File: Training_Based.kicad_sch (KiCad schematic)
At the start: 6 parts

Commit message: update
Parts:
- added K (x2): FINDER-36.11, Relay_THT:Relay_SPDT_Finder_36.11, symbol Relay:FINDER-36.11
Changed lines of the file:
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@@
     (pin "1")
+  )
+  (symbol (lib_id "Relay:FINDER-36.11") (at 52.705 45.085 0) (unit 1)
+    (in_bom yes) (on_board yes) (fields_autoplaced)
+    (default_instance (reference "K") (unit 1) (value "FINDER-36.11") (footprint "Relay_THT:Relay_SPDT_Finder_36.11"))
+    (property "Reference" "K" (id 0) (at 64.77 44.45 0)
+      (effects (font (size 1.27 1.27)) (justify left))
+    )
+    (property "Value" "FINDER-36.11" (id 1) (at 64.77 46.99 0)
+      (effects (font (size 1.27 1.27)) (justify left))
+    )
+    (property "Footprint" "Relay_THT:Relay_SPDT_Finder_36.11" (id 2) (at 84.963 45.847 0)
+      (effects (font (size 1.27 1.27)) hide)
+    )
+    (property "Datasheet" "https://gfinder.findernet.com/public/attachments/36/EN/S36EN.pdf" (id 3) (at 52.705 45.085 0)
+      (effects (font (size 1.27 1.27)) hide)
+    )
+    (pin "11")
+    (pin "12")
+    (pin "14")
+    (pin "A1")
+    (pin "A2")
   )
   (symbol (lib_id "power:GND") (at 255.905 150.495 0) (unit 1)
@@
     (pin "1")
   )
+  (symbol (lib_id "Relay:FINDER-36.11") (at 52.705 64.77 0) (unit 1)
+    (in_bom yes) (on_board yes) (fields_autoplaced)
+    (default_instance (reference "K") (unit 1) (value "FINDER-36.11") (footprint "Relay_THT:Relay_SPDT_Finder_36.11"))
+    (property "Reference" "K" (id 0) (at 64.77 64.135 0)
+      (effects (font (size 1.27 1.27)) (justify left))
+    )
+    (property "Value" "FINDER-36.11" (id 1) (at 64.77 66.675 0)
+      (effects (font (size 1.27 1.27)) (justify left))
+    )
+    (property "Footprint" "Relay_THT:Relay_SPDT_Finder_36.11" (id 2) (at 84.963 65.532 0)
+      (effects (font (size 1.27 1.27)) hide)
+    )
+    (property "Datasheet" "https://gfinder.findernet.com/public/attachments/36/EN/S36EN.pdf" (id 3) (at 52.705 64.77 0)
+      (effects (font (size 1.27 1.27)) hide)
+    )
+    (pin "11")
+    (pin "12")
+    (pin "14")
+    (pin "A1")
+    (pin "A2")
+  )
   (sheet_instances
     (path "/" (page "1"))
@@
       (reference "H6") (unit 1) (value "MountingHole_Pad") (footprint "MountingHole:MountingHole_3.2mm_M3_Pad_Via")
     )
+    (path "/0bf7dc38-c684-4e7e-b8ab-62403329c020"
+      (reference "K1") (unit 1) (value "FINDER-36.11") (footprint "Relay_THT:Relay_SPDT_Finder_36.11")
+    )
+    (path "/f917dee2-fb9b-4968-83ae-cd84153be184"
+      (reference "K2") (unit 1) (value "FINDER-36.11") (footprint "Relay_THT:Relay_SPDT_Finder_36.11")
+    )
   )

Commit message: update
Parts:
- added BZ: Buzzer, symbol Device:Buzzer
- added U: HC-SR04, symbol hc-sr04:HC-SR04
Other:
- moved on the sheet: K
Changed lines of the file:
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@@
     (pin "1")
   )
-  (symbol (lib_id "Relay:FINDER-36.11") (at 52.705 45.085 0) (unit 1)
+  (symbol (lib_id "Relay:FINDER-36.11") (at 52.705 46.99 0) (unit 1)
     (in_bom yes) (on_board yes) (fields_autoplaced)
     (default_instance (reference "K") (unit 1) (value "FINDER-36.11") (footprint "Relay_THT:Relay_SPDT_Finder_36.11"))
-    (property "Reference" "K" (id 0) (at 64.77 44.45 0)
-      (effects (font (size 1.27 1.27)) (justify left))
-    )
-    (property "Value" "FINDER-36.11" (id 1) (at 64.77 46.99 0)
-      (effects (font (size 1.27 1.27)) (justify left))
-    )
-    (property "Footprint" "Relay_THT:Relay_SPDT_Finder_36.11" (id 2) (at 84.963 45.847 0)
-      (effects (font (size 1.27 1.27)) hide)
-    )
-    (property "Datasheet" "https://gfinder.findernet.com/public/attachments/36/EN/S36EN.pdf" (id 3) (at 52.705 45.085 0)
+    (property "Reference" "K" (id 0) (at 64.77 46.355 0)
+      (effects (font (size 1.27 1.27)) (justify left))
+    )
+    (property "Value" "FINDER-36.11" (id 1) (at 64.77 48.895 0)
+      (effects (font (size 1.27 1.27)) (justify left))
+    )
+    (property "Footprint" "Relay_THT:Relay_SPDT_Finder_36.11" (id 2) (at 84.963 47.752 0)
+      (effects (font (size 1.27 1.27)) hide)
+    )
+    (property "Datasheet" "https://gfinder.findernet.com/public/attachments/36/EN/S36EN.pdf" (id 3) (at 52.705 46.99 0)
       (effects (font (size 1.27 1.27)) hide)
     )
@@
     (pin "1")
   )
+  (symbol (lib_id "Device:Buzzer") (at 146.685 47.625 0) (unit 1)
+    (in_bom yes) (on_board yes) (fields_autoplaced)
+    (default_instance (reference "BZ") (unit 1) (value "Buzzer") (footprint ""))
+    (property "Reference" "BZ" (id 0) (at 151.13 46.99 0)
+      (effects (font (size 1.27 1.27)) (justify left))
+    )
+    (property "Value" "Buzzer" (id 1) (at 151.13 49.53 0)
+      (effects (font (size 1.27 1.27)) (justify left))
+    )
+    (property "Footprint" "" (id 2) (at 146.05 45.085 90)
+      (effects (font (size 1.27 1.27)) hide)
+    )
+    (property "Datasheet" "~" (id 3) (at 146.05 45.085 90)
+      (effects (font (size 1.27 1.27)) hide)
+    )
+    (pin "1")
+    (pin "2")
+  )
   (symbol (lib_id "Mechanical:MountingHole_Pad") (at 261.62 130.81 270) (unit 1)
     (in_bom yes) (on_board yes)
@@
     )
     (pin "1")
+  )
+  (symbol (lib_id "hc-sr04:HC-SR04") (at 114.3 50.165 0) (unit 1)
+    (in_bom yes) (on_board yes)
+    (default_instance (reference "U") (unit 1) (value "HC-SR04") (footprint ""))
+    (property "Reference" "U" (id 0) (at 123.19 48.895 0)
+      (effects (font (size 1.524 1.524)) (justify left))
+    )
+    (property "Value" "HC-SR04" (id 1) (at 123.19 51.435 0)
+      (effects (font (size 1.524 1.524)) (justify left))
+    )
+    (property "Footprint" "" (id 2) (at 114.935 43.815 0)
+      (effects (font (size 1.524 1.524)))
+    )
+    (property "Datasheet" "" (id 3) (at 116.84 48.895 0)
+      (effects (font (size 1.524 1.524)))
+    )
+    (pin "~")
+    (pin "~")
+    (pin "~")
+    (pin "~")
   )
   (symbol (lib_id "Mechanical:MountingHole_Pad") (at 261.62 125.095 270) (unit 1)
@@
       (reference "#PWR01") (unit 1) (value "GND") (footprint "")
     )
+    (path "/4b249d15-dc1f-4ea2-a810-eeeb52784c39"
+      (reference "BZ1") (unit 1) (value "Buzzer") (footprint "Buzzer_Beeper:Buzzer_12x9.5RM7.6")
+    )
     (path "/bec85d69-b4a6-498e-b897-830e44594378"
       (reference "H1") (unit 1) (value "MountingHole_Pad") (footprint "MountingHole:MountingHole_3.2mm_M3_Pad_Via")
@@
       (reference "K2") (unit 1) (value "FINDER-36.11") (footprint "Relay_THT:Relay_SPDT_Finder_36.11")
     )
-  )
+    (path "/66e603fb-b814-425a-a9e3-3759b5b268a1"
+      (reference "U1") (unit 1) (value "HC-SR04") (footprint "Library:HC-SR04")
+    )
+  )

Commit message: add spacerx6
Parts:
- added AFF (x2): LTS-6980HR, Display_7Segment:7SegmentLED_LTS6760_LTS6780, symbol Display_Character:LTS-6980HR
- added U: Protoboard, symbol Training_board:Protoboard
- added U: DHT11, Sensor:Aosong_DHT11_5.5x12.0_P2.54mm, symbol Sensor:DHT11
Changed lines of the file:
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@@
     (pin "A2")
+  )
+  (symbol (lib_id "Training_board:Protoboard") (at 53.975 104.14 0) (unit 1)
+    (in_bom yes) (on_board yes) (fields_autoplaced)
+    (default_instance (reference "U") (unit 1) (value "Protoboard") (footprint ""))
+    (property "Reference" "U" (id 0) (at 60.96 103.505 0)
+      (effects (font (size 1.27 1.27)) (justify left))
+    )
+    (property "Value" "Protoboard" (id 1) (at 60.96 106.045 0)
+      (effects (font (size 1.27 1.27)) (justify left))
+    )
+    (property "Footprint" "" (id 2) (at 53.975 104.14 0)
+      (effects (font (size 1.27 1.27)) hide)
+    )
+    (property "Datasheet" "" (id 3) (at 53.975 104.14 0)
+      (effects (font (size 1.27 1.27)) hide)
+    )
   )
   (symbol (lib_id "power:GND") (at 255.905 150.495 0) (unit 1)
@@
     (pin "~")
   )
+  (symbol (lib_id "Display_Character:LTS-6980HR") (at 127.635 93.345 0) (unit 1)
+    (in_bom yes) (on_board yes) (fields_autoplaced)
+    (default_instance (reference "AFF") (unit 1) (value "LTS-6980HR") (footprint "Display_7Segment:7SegmentLED_LTS6760_LTS6780"))
+    (property "Reference" "AFF" (id 0) (at 127.635 76.835 0)
+      (effects (font (size 1.27 1.27)))
+    )
+    (property "Value" "LTS-6980HR" (id 1) (at 127.635 79.375 0)
+      (effects (font (size 1.27 1.27)))
+    )
+    (property "Footprint" "Display_7Segment:7SegmentLED_LTS6760_LTS6780" (id 2) (at 127.635 108.585 0)
+      (effects (font (size 1.27 1.27)) hide)
+    )
+    (property "Datasheet" "http://datasheet.octopart.com/LTS-6960HR-Lite-On-datasheet-11803242.pdf" (id 3) (at 127.635 93.345 0)
+      (effects (font (size 1.27 1.27)) hide)
+    )
+    (pin "1")
+    (pin "10")
+    (pin "2")
+    (pin "3")
+    (pin "4")
+    (pin "5")
+    (pin "6")
+    (pin "7")
+    (pin "8")
+    (pin "9")
+  )
+  (symbol (lib_id "Sensor:DHT11") (at 142.875 31.75 0) (unit 1)
+    (in_bom yes) (on_board yes) (fields_autoplaced)
+    (default_instance (reference "U") (unit 1) (value "DHT11") (footprint "Sensor:Aosong_DHT11_5.5x12.0_P2.54mm"))
+    (property "Reference" "U" (id 0) (at 135.89 31.115 0)
+      (effects (font (size 1.27 1.27)) (justify right))
+    )
+    (property "Value" "DHT11" (id 1) (at 135.89 33.655 0)
+      (effects (font (size 1.27 1.27)) (justify right))
+    )
+    (property "Footprint" "Sensor:Aosong_DHT11_5.5x12.0_P2.54mm" (id 2) (at 142.875 41.91 0)
+      (effects (font (size 1.27 1.27)) hide)
+    )
+    (property "Datasheet" "http://akizukidenshi.com/download/ds/aosong/DHT11.pdf" (id 3) (at 146.685 25.4 0)
+      (effects (font (size 1.27 1.27)) hide)
+    )
+    (pin "1")
+    (pin "2")
+    (pin "3")
+    (pin "4")
+  )
   (symbol (lib_id "Mechanical:MountingHole_Pad") (at 261.62 125.095 270) (unit 1)
     (in_bom yes) (on_board yes)
@@
     )
     (pin "1")
+  )
+  (symbol (lib_id "Display_Character:LTS-6980HR") (at 95.885 92.71 0) (unit 1)
+    (in_bom yes) (on_board yes) (fields_autoplaced)
+    (default_instance (reference "AFF") (unit 1) (value "LTS-6980HR") (footprint "Display_7Segment:7SegmentLED_LTS6760_LTS6780"))
+    (property "Reference" "AFF" (id 0) (at 95.885 76.2 0)
+      (effects (font (size 1.27 1.27)))
+    )
+    (property "Value" "LTS-6980HR" (id 1) (at 95.885 78.74 0)
+      (effects (font (size 1.27 1.27)))
+    )
+    (property "Footprint" "Display_7Segment:7SegmentLED_LTS6760_LTS6780" (id 2) (at 95.885 107.95 0)
+      (effects (font (size 1.27 1.27)) hide)
+    )
+    (property "Datasheet" "http://datasheet.octopart.com/LTS-6960HR-Lite-On-datasheet-11803242.pdf" (id 3) (at 95.885 92.71 0)
+      (effects (font (size 1.27 1.27)) hide)
+    )
+    (pin "1")
+    (pin "10")
+    (pin "2")
+    (pin "3")
+    (pin "4")
+    (pin "5")
+    (pin "6")
+    (pin "7")
+    (pin "8")
+    (pin "9")
   )
   (symbol (lib_id "Relay:FINDER-36.11") (at 52.705 64.77 0) (unit 1)
@@
       (reference "#PWR01") (unit 1) (value "GND") (footprint "")
     )
+    (path "/d28ba196-9e7b-40b2-b3ef-8cb68851e10f"
+      (reference "AFF1") (unit 1) (value "LTS-6980HR") (footprint "Display_7Segment:7SegmentLED_LTS6760_LTS6780")
+    )
+    (path "/9d925192-1582-48c4-b69c-59437c278f89"
+      (reference "AFF2") (unit 1) (value "LTS-6980HR") (footprint "Display_7Segment:7SegmentLED_LTS6760_LTS6780")
+    )
     (path "/4b249d15-dc1f-4ea2-a810-eeeb52784c39"
       (reference "BZ1") (unit 1) (value "Buzzer") (footprint "Buzzer_Beeper:Buzzer_12x9.5RM7.6")
@@
       (reference "U1") (unit 1) (value "HC-SR04") (footprint "Library:HC-SR04")
     )
-  )
+    (path "/a1b2256e-71d9-455c-a704-d555bf14e270"
+      (reference "U2") (unit 1) (value "DHT11") (footprint "Sensor:Aosong_DHT11_5.5x12.0_P2.54mm")
+    )
+    (path "/17077e5b-82a4-4c35-a7b1-ed0c3a3a0da8"
+      (reference "U3") (unit 1) (value "Protoboard") (footprint "Library:Protoboard")
+    )
+  )

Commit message: ีWork in Progress
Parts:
- removed U (x2): (no value), symbol Mechanical:MountingHole_Pad
- removed U: DHT11, Sensor:Aosong_DHT11_5.5x12.0_P2.54mm, symbol Sensor:DHT11
- added J (x4): Conn_01x19, symbol Connector_Generic:Conn_01x19
- added PIR: PIR_Motion_Sensor, symbol sensors:PIR_Motion_Sensor
- added Q: BC817, Package_TO_SOT_SMD:SOT-23, symbol Transistor_BJT:BC817
- added TH: DHT11_Temperature_Humidity, symbol sensors:DHT11_Temperature_Humidity
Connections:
- net GND: now also Q.2 (E)
- net +5V: now reaches BZ.1 (-)
- net at BZ.2 (+): now also Q.3 (C)
- new net: J.1 (Pin_1), J.1 (Pin_1) (x2)
- new net: J.10 (Pin_10), J.10 (Pin_10) (x2)
- new net: J.11 (Pin_11), J.11 (Pin_11) (x2)
- new net: J.12 (Pin_12), J.12 (Pin_12) (x2)
- new net: J.13 (Pin_13), J.13 (Pin_13) (x2)
- new net: J.14 (Pin_14), J.14 (Pin_14) (x2)
- new net: J.15 (Pin_15), J.15 (Pin_15) (x2)
- new net: J.16 (Pin_16), J.16 (Pin_16) (x2)
- new net: J.17 (Pin_17), J.17 (Pin_17) (x2)
- new net: J.18 (Pin_18), J.18 (Pin_18) (x2)
- new net: J.19 (Pin_19), J.19 (Pin_19) (x2)
- new net: J.2 (Pin_2), J.2 (Pin_2) (x2)
- new net: J.3 (Pin_3), J.3 (Pin_3) (x2)
- new net: J.4 (Pin_4), J.4 (Pin_4) (x2)
- new net: J.5 (Pin_5), J.5 (Pin_5) (x2)
- new net: J.6 (Pin_6), J.6 (Pin_6) (x2)
- new net: J.7 (Pin_7), J.7 (Pin_7) (x2)
- new net: J.8 (Pin_8), J.8 (Pin_8) (x2)
- new net: J.9 (Pin_9), J.9 (Pin_9) (x2)
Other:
- moved on the sheet: AFF, BZ, K, U

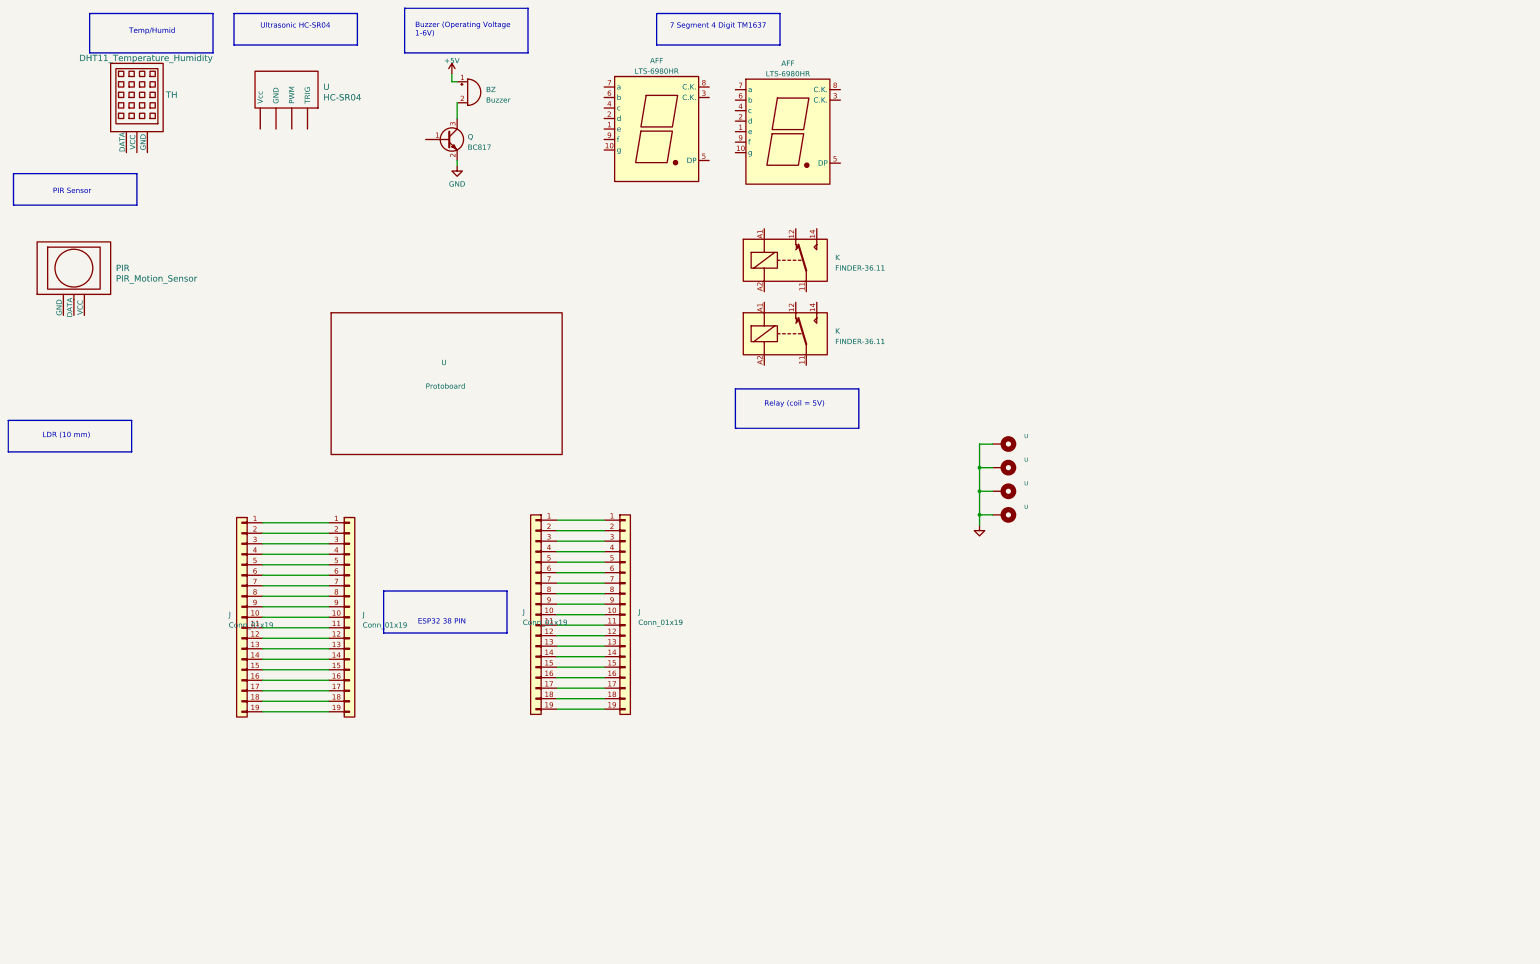
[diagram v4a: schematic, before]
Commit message: add esp32 board and 3d model
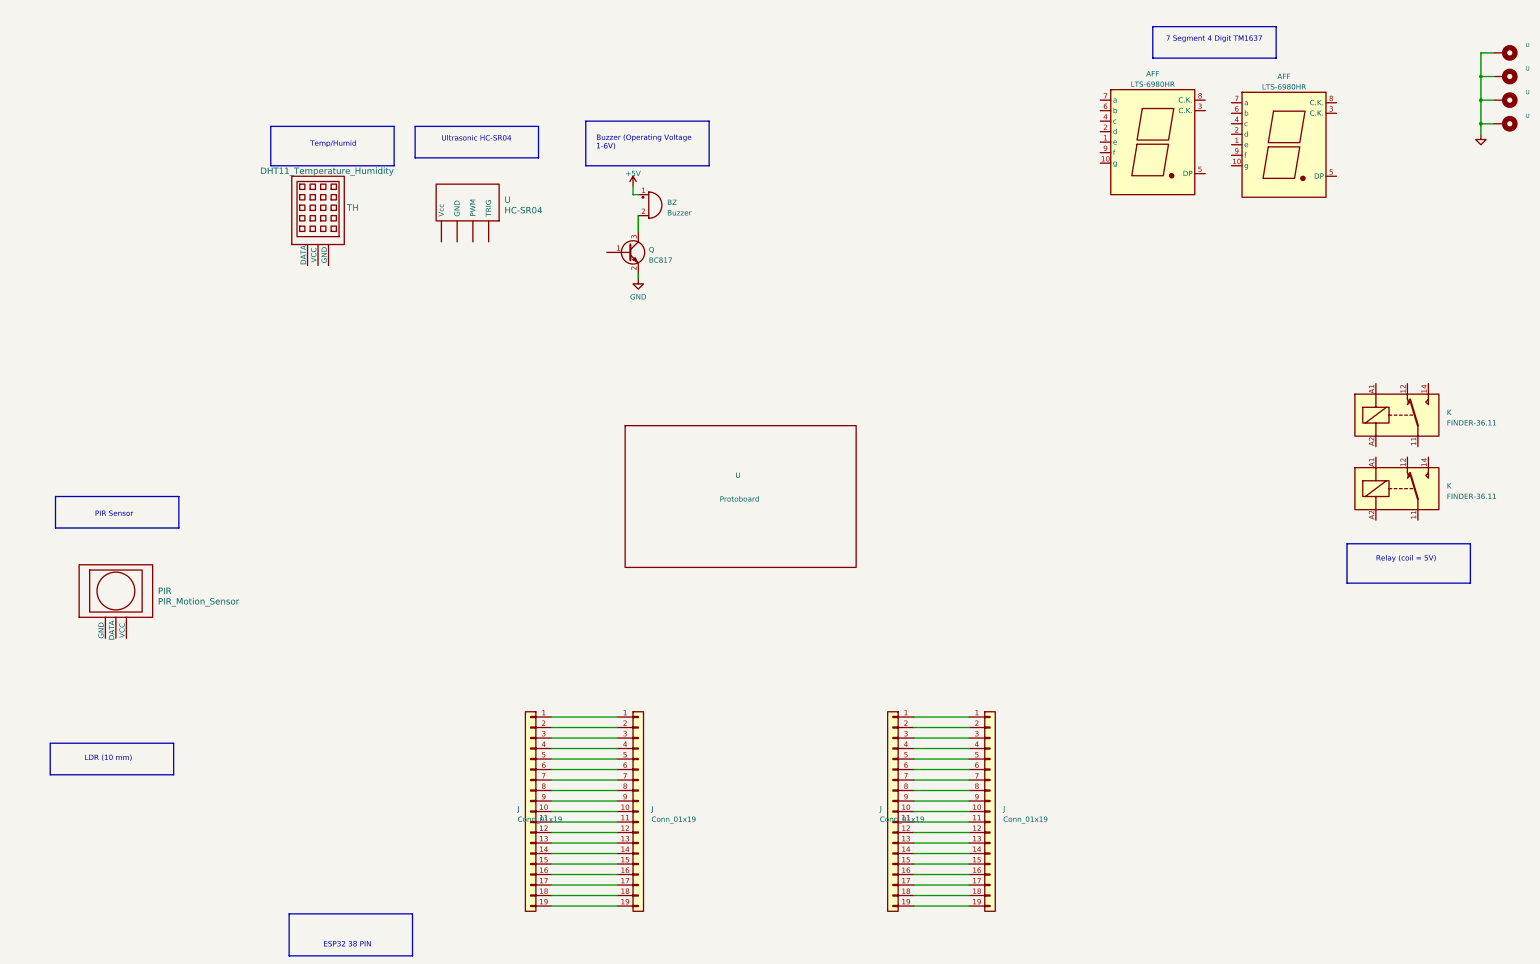
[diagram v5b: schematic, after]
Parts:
- removed J (x2): Conn_01x19, symbol Connector_Generic:Conn_01x19
- added J (x2): Conn_01x19, symbol Connector_Generic:Conn_01x19
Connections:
- net at J.1 (Pin_1): now also J.1 (Pin_1) (x2)
- net at J.10 (Pin_10): now also J.10 (Pin_10) (x2)
- net at J.11 (Pin_11): now also J.11 (Pin_11) (x2)
- net at J.12 (Pin_12): now also J.12 (Pin_12) (x2)
- net at J.13 (Pin_13): now also J.13 (Pin_13) (x2)
- net at J.14 (Pin_14): now also J.14 (Pin_14) (x2)
- net at J.15 (Pin_15): now also J.15 (Pin_15) (x2)
- net at J.16 (Pin_16): now also J.16 (Pin_16) (x2)
- net at J.17 (Pin_17): now also J.17 (Pin_17) (x2)
- net at J.18 (Pin_18): now also J.18 (Pin_18) (x2)
- net at J.19 (Pin_19): now also J.19 (Pin_19) (x2)
- net at J.2 (Pin_2): now also J.2 (Pin_2) (x2)
- net at J.3 (Pin_3): now also J.3 (Pin_3) (x2)
- net at J.4 (Pin_4): now also J.4 (Pin_4) (x2)
- net at J.5 (Pin_5): now also J.5 (Pin_5) (x2)
- net at J.6 (Pin_6): now also J.6 (Pin_6) (x2)
- net at J.7 (Pin_7): now also J.7 (Pin_7) (x2)
- net at J.8 (Pin_8): now also J.8 (Pin_8) (x2)
- net at J.9 (Pin_9): now also J.9 (Pin_9) (x2)
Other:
- moved on the sheet: AFF, BZ, J, K, PIR, Q, TH, U
